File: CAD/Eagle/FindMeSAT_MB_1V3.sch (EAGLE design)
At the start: 135 parts, among them Q101 ABS07-32.768KHZ, Q651 ABM3B-16MHZ-10-R50-1-U, U1001 CFPT-141-20MHZ, U101 ATXMEGA256A3BU-AU, U1011 OPA354, U1021 OPA354, U1111 LM2831YMF, U1121 LM4120IM5-3.0, U201 SIM808, U301 MPU-9250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

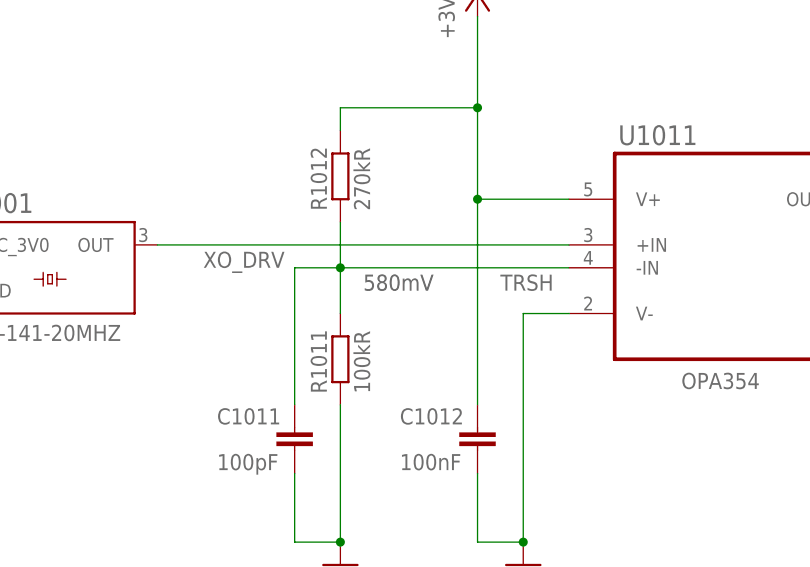
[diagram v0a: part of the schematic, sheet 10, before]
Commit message: HW_V1.3 - C1001: PWM 100nF changed to 10uF with SMD0805 footprint
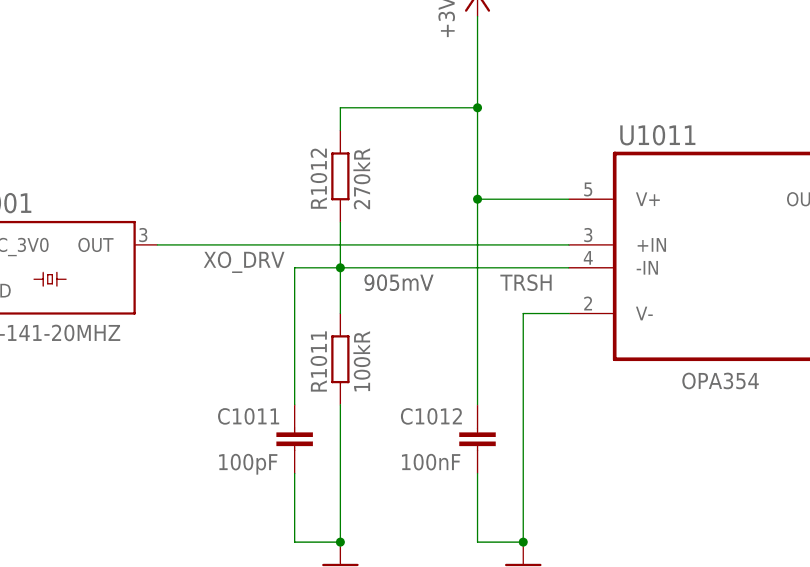
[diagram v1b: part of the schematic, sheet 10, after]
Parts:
- C1001: device rcl:C-EUC0603 -> rcl:C-EUC0805
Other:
- note added: "905mV"
- note removed: "580mV"
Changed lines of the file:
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@@
 <part name="C1002" library="rcl" deviceset="C-EU" device="C0603" value="100nF"/>
 <part name="+3V0_1001" library="df4iah_supply" deviceset="+3V0" device=""/>
-<part name="C1001" library="rcl" deviceset="C-EU" device="C0603" value="10uF"/>
+<part name="C1001" library="rcl" deviceset="C-EU" device="C0805" value="10uF"/>
 <part name="R1001" library="rcl" deviceset="R-EU_" device="R0603" value="100kR"/>
 <part name="GND1001" library="df4iah_supply" deviceset="GND" device=""/>
@@
 <pinref part="C251" gate="G$1" pin="1"/>
 <junction x="86.36" y="139.7"/>
+<label x="63.5" y="139.7" size="1.778" layer="95" rot="R270" xref="yes"/>
 </segment>
 </net>
@@
 <plain>
 <text x="35.56" y="127" size="1.778" layer="97">f_LP = 1 Hz, PWM min. 100 Hz</text>
-<text x="144.78" y="116.84" size="1.778" layer="97">580mV</text>
+<text x="144.78" y="116.84" size="1.778" layer="97">905mV</text>
 </plain>
 <instances>

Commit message: HW_V1.3 - U501 Hygro SHT31-DIS - nRESET to be disconnected, especially from GND
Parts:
- removed R1141: 4.02kR, rcl:R-EU_R0603
- added C1141: 100pF, rcl:C-EUC0603
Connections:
- removed net AD_3V0: R1141.2, R1142.1, U101A.PA0
- new net AREFA: C1141.1, R1142.1, U101A.PA0
- net GND: now also C1141.2; no longer R1141.1, U501.!RESET
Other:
- note added: "AREF for ADCA"
- note removed: "1:0.668 = 2V"
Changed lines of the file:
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@@
 <part name="R1111" library="rcl" deviceset="R-EU_" device="R0603" value="4.02kR"/>
 <part name="GND1112" library="df4iah_supply" deviceset="GND" device=""/>
-<part name="R1141" library="rcl" deviceset="R-EU_" device="R0603" value="4.02kR"/>
 <part name="GND1141" library="df4iah_supply" deviceset="GND" device=""/>
 <part name="U1021" library="df4iah_opamp" deviceset="OPA354" device=""/>
@@
 <part name="FM1204" library="df4iah_fiducial" deviceset="FIDUCIAL_MARK_1MM" device=""/>
 <part name="GND651" library="df4iah_supply" deviceset="GND" device=""/>
+<part name="C1141" library="rcl" deviceset="C-EU" device="C0603" value="100pF"/>
 </parts>
 <sheets>
@@
 </segment>
 </net>
-<net name="AD_3V0" class="0">
+<net name="AREFA" class="0">
 <segment>
 <wire x1="88.9" y1="139.7" x2="83.82" y2="139.7" width="0.1524" layer="91"/>
@@
 <junction x="182.88" y="111.76"/>
 <junction x="124.46" y="111.76"/>
-<wire x1="142.24" y1="93.98" x2="142.24" y2="88.9" width="0.1524" layer="91"/>
-<pinref part="U501" gate="G$1" pin="!RESET"/>
-<wire x1="142.24" y1="88.9" x2="137.16" y2="88.9" width="0.1524" layer="91"/>
-<junction x="142.24" y="93.98"/>
 </segment>
 </net>
@@
 <text x="139.7" y="134.62" size="1.778" layer="97">0.6V</text>
 <text x="55.88" y="154.94" size="1.778" layer="97">1:0.4 = 2.0V</text>
-<text x="233.68" y="35.56" size="1.778" layer="97">1:0.668 = 2V</text>
+<text x="233.68" y="35.56" size="1.778" layer="97">AREF for ADCA</text>
 <text x="226.06" y="154.94" size="1.778" layer="97">1:0.4 = 2.0V</text>
 </plain>
@@
 <instance part="R1111" gate="G$1" x="40.64" y="109.22" rot="R90"/>
 <instance part="GND1112" gate="1" x="40.64" y="99.06"/>
-<instance part="R1141" gate="G$1" x="215.9" y="38.1" rot="R90"/>
 <instance part="GND1141" gate="1" x="215.9" y="27.94"/>
 <instance part="R1132" gate="G$1" x="175.26" y="162.56"/>
 <instance part="R1131" gate="G$1" x="193.04" y="162.56"/>
 <instance part="GND1131" gate="1" x="203.2" y="157.48"/>
+<instance part="C1141" gate="G$1" x="215.9" y="38.1" smashed="yes">
+<attribute name="NAME" x="212.979" y="32.004" size="1.778" layer="95" rot="R90"/>
+<attribute name="VALUE" x="220.599" y="32.004" size="1.778" layer="96" rot="R90"/>
+</instance>
 </instances>
 <busses>
@@
 </segment>
 <segment>
-<pinref part="GND1141" gate="1" pin="GND"/>
-<pinref part="R1141" gate="G$1" pin="1"/>
-<wire x1="215.9" y1="30.48" x2="215.9" y2="33.02" width="0.1524" layer="91"/>
-</segment>
-<segment>
 <pinref part="R1131" gate="G$1" pin="2"/>
 <wire x1="198.12" y1="162.56" x2="203.2" y2="162.56" width="0.1524" layer="91"/>
 <wire x1="203.2" y1="162.56" x2="203.2" y2="160.02" width="0.1524" layer="91"/>
 <pinref part="GND1131" gate="1" pin="GND"/>
+</segment>
+<segment>
+<pinref part="GND1141" gate="1" pin="GND"/>
+<pinref part="C1141" gate="G$1" pin="2"/>
+<wire x1="215.9" y1="30.48" x2="215.9" y2="33.02" width="0.1524" layer="91"/>
 </segment>
 </net>
@@
 </segment>
 </net>
-<net name="AD_3V0" class="0">
-<segment>
-<wire x1="220.98" y1="43.18" x2="220.98" y2="33.02" width="0.1524" layer="91"/>
-<wire x1="220.98" y1="33.02" x2="231.14" y2="33.02" width="0.1524" layer="91"/>
+<net name="AREFA" class="0">
+<segment>
+<wire x1="223.52" y1="43.18" x2="223.52" y2="33.02" width="0.1524" layer="91"/>
+<wire x1="223.52" y1="33.02" x2="231.14" y2="33.02" width="0.1524" layer="91"/>
 <label x="231.14" y="33.02" size="1.778" layer="97" xref="yes"/>
 <pinref part="R1142" gate="G$1" pin="1"/>
-<pinref part="R1141" gate="G$1" pin="2"/>
 <wire x1="215.9" y1="43.18" x2="215.9" y2="45.72" width="0.1524" layer="91"/>
-<wire x1="220.98" y1="43.18" x2="215.9" y2="43.18" width="0.1524" layer="91"/>
+<wire x1="223.52" y1="43.18" x2="215.9" y2="43.18" width="0.1524" layer="91"/>
 <junction x="215.9" y="43.18"/>
-</segment>
-</net>
+<pinref part="C1141" gate="G$1" pin="1"/>
+<wire x1="215.9" y1="43.18" x2="215.9" y2="40.64" width="0.1524" layer="91"/>
+</segment>
+</net>

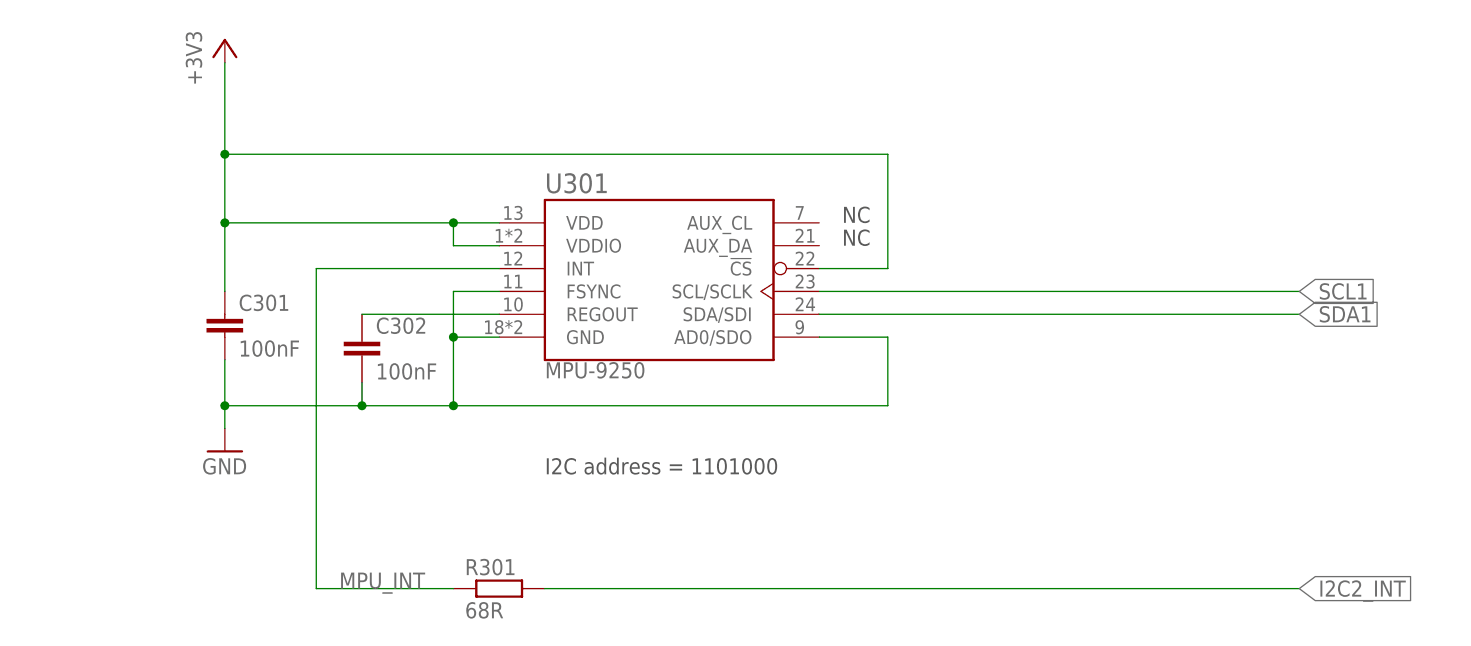
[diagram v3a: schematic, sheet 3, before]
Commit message: HW_V1.3 - Version strings changed to V1.3, missing C302 with 10nF added, missing GND vias for U201 added (4x)
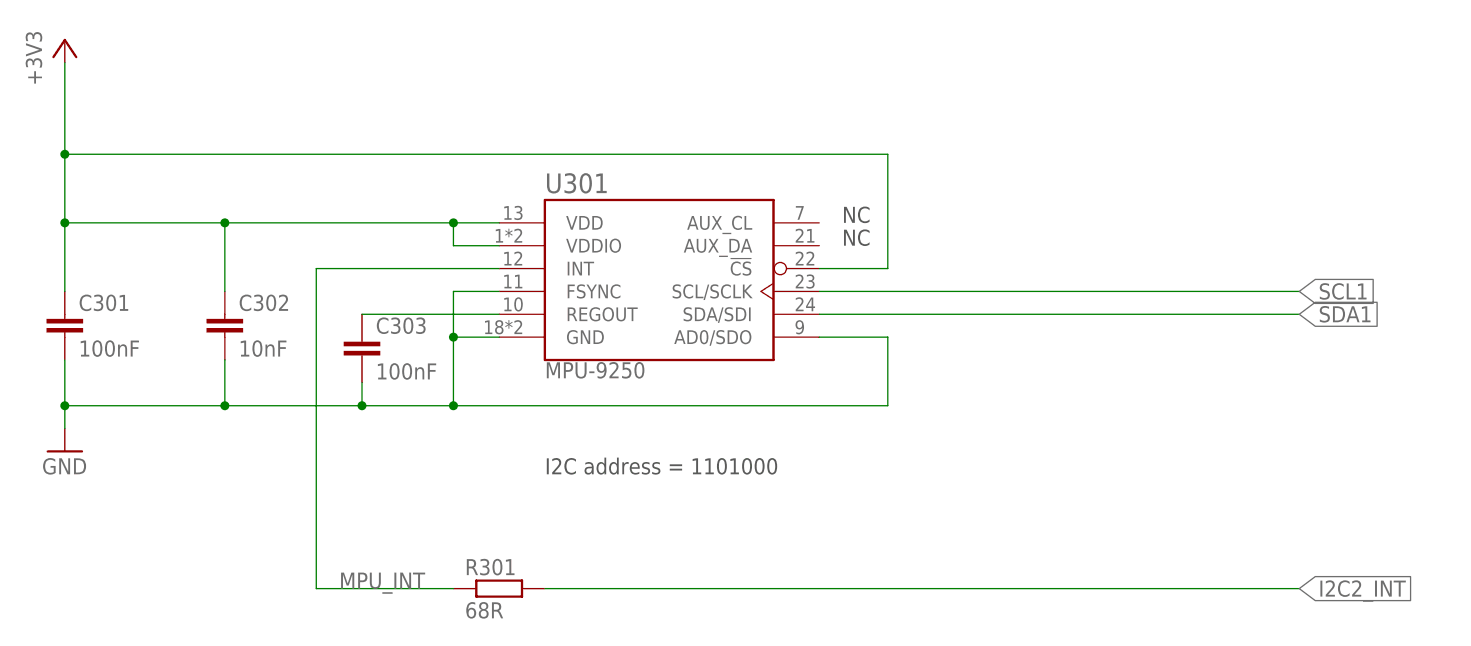
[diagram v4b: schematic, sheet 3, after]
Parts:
- added C303: 100nF, rcl:C-EUC0603
- C302: value 100nF -> 10nF
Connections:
- net +3V3: now also C302.1
- net GAM_RO: now also C303.1; no longer C302.1
- net GND: now also C303.2
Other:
- moved on the sheet: C301, C302
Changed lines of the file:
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@@
 <part name="+3V3_311" library="df4iah_supply" deviceset="+3V3" device=""/>
 <part name="C301" library="rcl" deviceset="C-EU" device="C0603" value="100nF"/>
-<part name="C302" library="rcl" deviceset="C-EU" device="C0603" value="100nF"/>
+<part name="C303" library="rcl" deviceset="C-EU" device="C0603" value="100nF"/>
 <part name="GND401" library="df4iah_supply" deviceset="GND" device=""/>
 <part name="+3V3_401" library="df4iah_supply" deviceset="+3V3" device=""/>
@@
 <part name="GND651" library="df4iah_supply" deviceset="GND" device=""/>
 <part name="C1141" library="rcl" deviceset="C-EU" device="C0603" value="100pF"/>
+<part name="C302" library="rcl" deviceset="C-EU" device="C0603" value="10nF"/>
 </parts>
 <sheets>
@@
 <attribute name="VALUE" x="116.84" y="86.106" size="1.778" layer="96" font="vector" align="top-left"/>
 </instance>
-<instance part="GND311" gate="1" x="81.28" y="76.2"/>
-<instance part="+3V3_311" gate="G$1" x="81.28" y="121.92"/>
-<instance part="C301" gate="G$1" x="81.28" y="91.44"/>
-<instance part="C302" gate="G$1" x="96.52" y="88.9"/>
+<instance part="GND311" gate="1" x="63.5" y="76.2"/>
+<instance part="+3V3_311" gate="G$1" x="63.5" y="121.92"/>
+<instance part="C301" gate="G$1" x="63.5" y="91.44"/>
+<instance part="C303" gate="G$1" x="96.52" y="88.9"/>
 <instance part="R301" gate="G$1" x="111.76" y="60.96"/>
+<instance part="C302" gate="G$1" x="81.28" y="91.44"/>
 </instances>
 <busses>
@@
 <segment>
 <pinref part="GND311" gate="1" pin="GND"/>
-<wire x1="81.28" y1="78.74" x2="81.28" y2="81.28" width="0.1524" layer="91"/>
+<wire x1="63.5" y1="78.74" x2="63.5" y2="81.28" width="0.1524" layer="91"/>
 <pinref part="U301" gate="G$1" pin="AD0/SDO"/>
 <wire x1="154.94" y1="88.9" x2="147.32" y2="88.9" width="0.1524" layer="91"/>
 <wire x1="154.94" y1="81.28" x2="154.94" y2="88.9" width="0.1524" layer="91"/>
+<wire x1="63.5" y1="81.28" x2="81.28" y2="81.28" width="0.1524" layer="91"/>
+<junction x="63.5" y="81.28"/>
+<pinref part="C301" gate="G$1" pin="2"/>
 <wire x1="81.28" y1="81.28" x2="96.52" y2="81.28" width="0.1524" layer="91"/>
-<junction x="81.28" y="81.28"/>
-<pinref part="C301" gate="G$1" pin="2"/>
 <wire x1="96.52" y1="81.28" x2="106.68" y2="81.28" width="0.1524" layer="91"/>
 <wire x1="106.68" y1="81.28" x2="154.94" y2="81.28" width="0.1524" layer="91"/>
-<wire x1="81.28" y1="81.28" x2="81.28" y2="86.36" width="0.1524" layer="91"/>
+<wire x1="63.5" y1="81.28" x2="63.5" y2="86.36" width="0.1524" layer="91"/>
 <pinref part="U301" gate="G$1" pin="GND"/>
 <wire x1="111.76" y1="88.9" x2="106.68" y2="88.9" width="0.1524" layer="91"/>
@@
 <junction x="106.68" y="81.28"/>
 <junction x="106.68" y="88.9"/>
-<pinref part="C302" gate="G$1" pin="2"/>
+<pinref part="C303" gate="G$1" pin="2"/>
 <wire x1="96.52" y1="81.28" x2="96.52" y2="83.82" width="0.1524" layer="91"/>
 <junction x="96.52" y="81.28"/>
+<pinref part="C302" gate="G$1" pin="2"/>
+<wire x1="81.28" y1="81.28" x2="81.28" y2="86.36" width="0.1524" layer="91"/>
+<junction x="81.28" y="81.28"/>
 </segment>
 </net>
@@
 <segment>
 <pinref part="+3V3_311" gate="G$1" pin="+3V3"/>
-<wire x1="81.28" y1="119.38" x2="81.28" y2="109.22" width="0.1524" layer="91"/>
-<wire x1="81.28" y1="109.22" x2="81.28" y2="101.6" width="0.1524" layer="91"/>
+<wire x1="63.5" y1="119.38" x2="63.5" y2="109.22" width="0.1524" layer="91"/>
+<wire x1="63.5" y1="109.22" x2="63.5" y2="101.6" width="0.1524" layer="91"/>
+<wire x1="63.5" y1="101.6" x2="81.28" y2="101.6" width="0.1524" layer="91"/>
+<pinref part="U301" gate="G$1" pin="VDDIO"/>
 <wire x1="81.28" y1="101.6" x2="106.68" y2="101.6" width="0.1524" layer="91"/>
-<pinref part="U301" gate="G$1" pin="VDDIO"/>
 <wire x1="106.68" y1="101.6" x2="106.68" y2="99.06" width="0.1524" layer="91"/>
 <wire x1="106.68" y1="99.06" x2="111.76" y2="99.06" width="0.1524" layer="91"/>
@@
 <junction x="106.68" y="101.6"/>
 <pinref part="C301" gate="G$1" pin="1"/>
-<wire x1="81.28" y1="101.6" x2="81.28" y2="93.98" width="0.1524" layer="91"/>
-<junction x="81.28" y="101.6"/>
-<wire x1="81.28" y1="109.22" x2="154.94" y2="109.22" width="0.1524" layer="91"/>
+<wire x1="63.5" y1="101.6" x2="63.5" y2="93.98" width="0.1524" layer="91"/>
+<junction x="63.5" y="101.6"/>
+<wire x1="63.5" y1="109.22" x2="154.94" y2="109.22" width="0.1524" layer="91"/>
 <wire x1="154.94" y1="109.22" x2="154.94" y2="96.52" width="0.1524" layer="91"/>
 <pinref part="U301" gate="G$1" pin="!CS"/>
 <wire x1="154.94" y1="96.52" x2="147.32" y2="96.52" width="0.1524" layer="91"/>
-<junction x="81.28" y="109.22"/>
+<junction x="63.5" y="109.22"/>
+<pinref part="C302" gate="G$1" pin="1"/>
+<wire x1="81.28" y1="101.6" x2="81.28" y2="93.98" width="0.1524" layer="91"/>
+<junction x="81.28" y="101.6"/>
 </segment>
 </net>
@@
 <segment>
 <pinref part="U301" gate="G$1" pin="REGOUT"/>
-<pinref part="C302" gate="G$1" pin="1"/>
+<pinref part="C303" gate="G$1" pin="1"/>
 <wire x1="111.76" y1="91.44" x2="96.52" y2="91.44" width="0.1524" layer="91"/>
 </segment>
